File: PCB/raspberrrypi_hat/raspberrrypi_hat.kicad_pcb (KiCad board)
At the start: 4 copper layers, 65 x 56 mm, 32 parts, among them J1 40HAT, J2 CONN_02X02, J3 CONN_01X02, J4 Micro_SIM_Card, Q1 DMG2305UX, Q2 DMMT5401, U1 CAT24C32, U2 NeowayM590

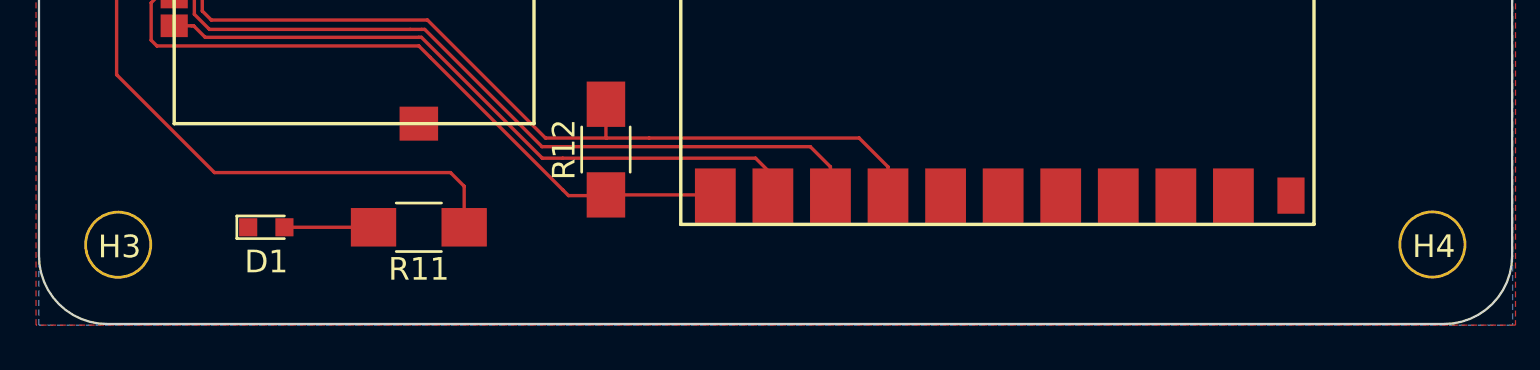
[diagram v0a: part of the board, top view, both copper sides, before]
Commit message: PCB: Add description on F.Silks. IOTilt M590 GSM/GPRS Raspberry pi HAT
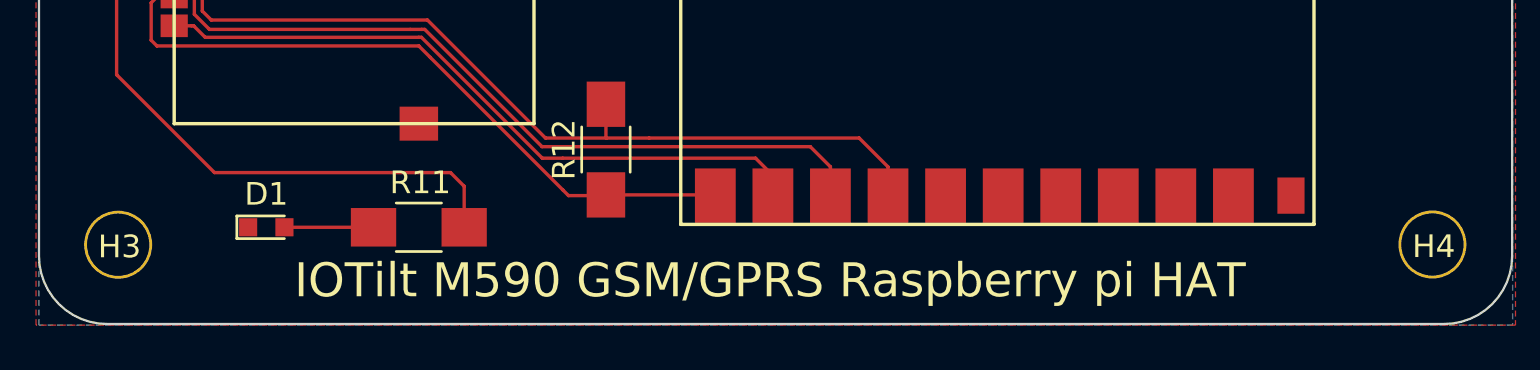
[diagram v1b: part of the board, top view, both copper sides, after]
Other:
- board text added: "IOTilt M590 GSM/GPRS Raspberry pi HAT"
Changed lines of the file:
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@@
     (area 74.244762 54 229.685714 128.300001)
     (thickness 1.6)
-    (drawings 53)
+    (drawings 54)
     (tracks 198)
     (zones 0)
@@
     (tags "resistor 1206")
     (attr smd)
-    (fp_text reference R11 (at 0 -1.85 180) (layer F.SilkS)
+    (fp_text reference R11 (at -0.0635 1.9685 180) (layer F.SilkS)
       (effects (font (size 1 1) (thickness 0.15)))
     )
@@
     (tags "LED led 0603 SMD smd SMT smt smdled SMDLED smtled SMTLED")
     (attr smd)
-    (fp_text reference D1 (at 0 1.524) (layer F.SilkS)
+    (fp_text reference D1 (at 0 -1.4605) (layer F.SilkS)
       (effects (font (size 1 1) (thickness 0.15)))
     )
@@
       (net 1 GND))
   )
+  (gr_text "IOTilt M590 GSM/GPRS Raspberry pi HAT" (at 110.801 114.8995) (layer F.SilkS)
+    (effects (font (size 1.5 1.5) (thickness 0.3)))
+  )
   (gr_text "This is a HAT compatible PCB starting design based on the official\nRaspberry Pi specs at:\nhttps://github.com/raspberrypi/hats/blob/master/designguide.md\n\nCurrently the camera slot and display cutout are not here. \nSee the schematic for the details on the EEPROM and power setup.\n\nThis board does have the correct components for powering the Pi via\nthe HAT. If you need the Pi to provide 5V or 3.3V, please remove or\nconnect the appropriate components." (at 189.4 83.7) (layer Cmts.User)

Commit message: PCB: Add version 0.1 on F.Silks
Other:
- board text added: "Version 0.1"
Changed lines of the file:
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@@
     (area 74.244762 54 229.685714 128.300001)
     (thickness 1.6)
-    (drawings 54)
+    (drawings 55)
     (tracks 198)
     (zones 0)
@@
       (net 1 GND))
   )
+  (gr_text "Version 0.1" (at 140.011 103.152 90) (layer F.SilkS)
+    (effects (font (size 1 1) (thickness 0.2)))
+  )
   (gr_text "IOTilt M590 GSM/GPRS Raspberry pi HAT" (at 110.801 114.8995) (layer F.SilkS)
